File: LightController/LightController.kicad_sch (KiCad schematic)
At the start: 0 parts

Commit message: Add the funky stuff to start.  This will be hell btw.
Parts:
- added J1: RJ45, symbol Connector:RJ45
- added Q1: BSS138, Package_TO_SOT_SMD:SOT-23, symbol Transistor_FET:BSS138
- added Q2, Q3, Q4, Q5, Q6, Q7: Q_NMOS_GDS, Package_TO_SOT_THT:TO-220-3_Vertical, symbol Device:Q_NMOS_GDS
- added R1, R2: 10k, symbol Device:R_US
- added R3, R4, R5, R6, R7, R8: 330ohm, symbol Device:R_US
- added U1: ESP32-WROOM-32D, RF_Module:ESP32-WROOM-32, symbol RF_Module:ESP32-WROOM-32D
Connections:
- new net: Q5.1 (G), R6.2
- new net: Q6.1 (G), R7.2
- new net: Q3.1 (G), R4.2
- new net: Q7.1 (G), R8.2
- new net: Q2.1 (G), R3.2
- new net: Q4.1 (G), R5.2
- new net GND: Q1.2 (S), Q1.3 (D), R1.2, R2.2, U1.1 (GND), U1.15 (GND), U1.38 (GND), U1.39 (GND)
- new net STATUS_LED: Q1.1 (G), R1.1, U1.12 (IO27)
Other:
- note added: "12V to 3.3V for ESP32"
- note added: "Main Brain"
- note added: "Output Channels"
- note added: "RS485 Comms"
- note added: "Sig/Pwr Input"
- note added: "Status LED Output (there is no 5v source on this board hahaha fuck!)"
- note added: "https://forum.arduino.cc/t/logic-level-converter-schematic/523295"
- company: (none) -> Garden State Combat Robotics League
- title: (none) -> LED Channel Controller

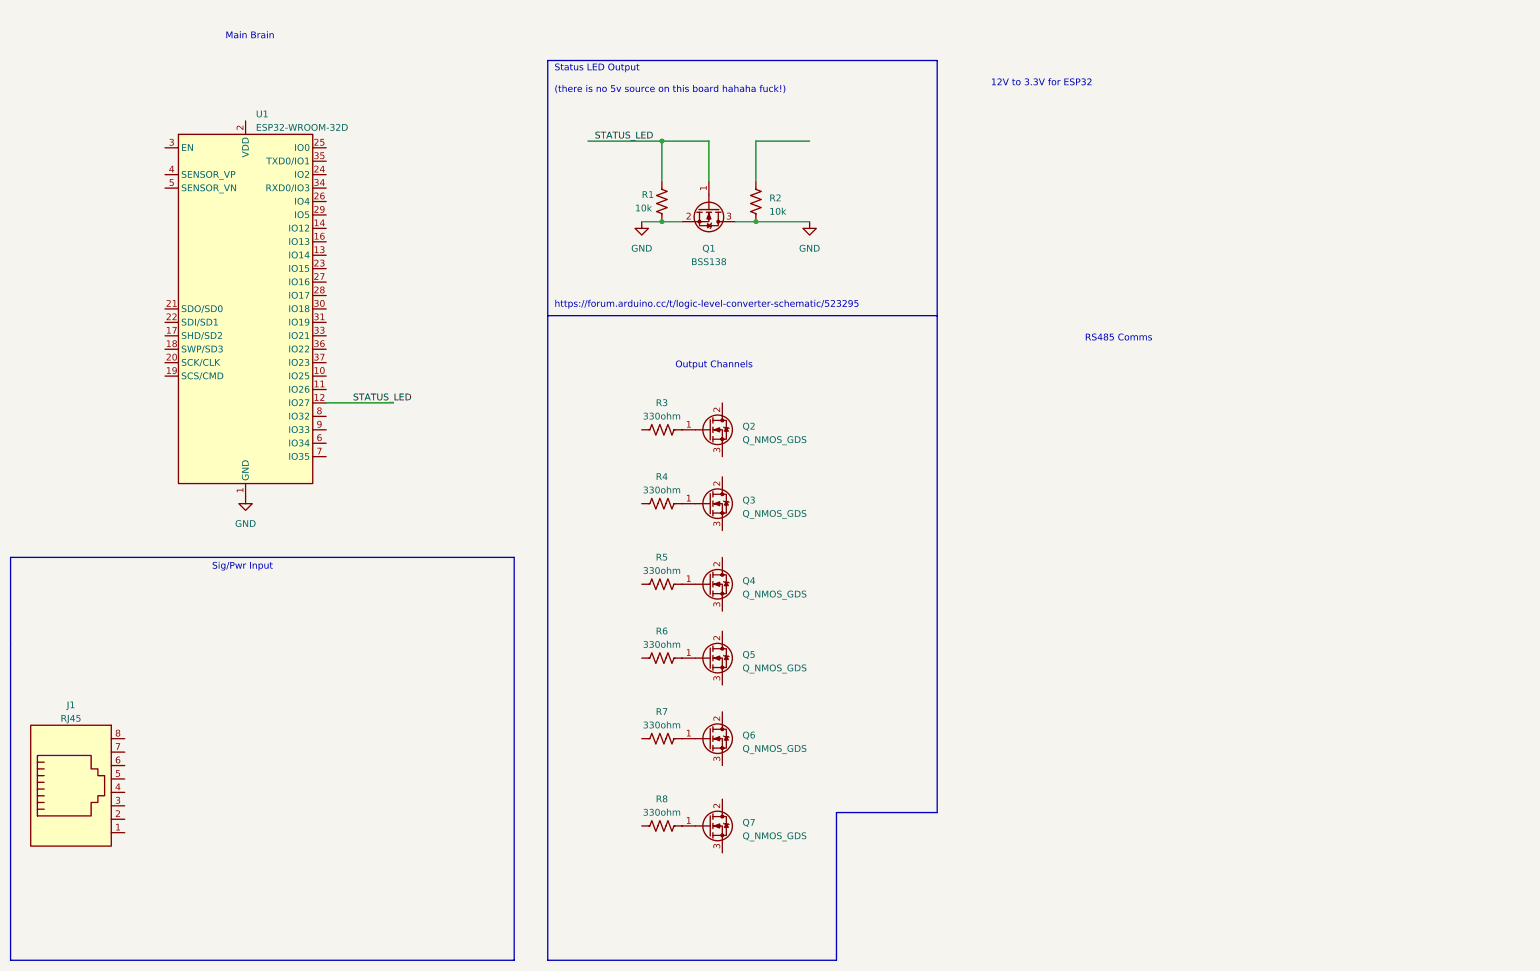
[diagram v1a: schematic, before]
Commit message: Updated first half of schematic, mostlyish.  Lots to go for lighting.
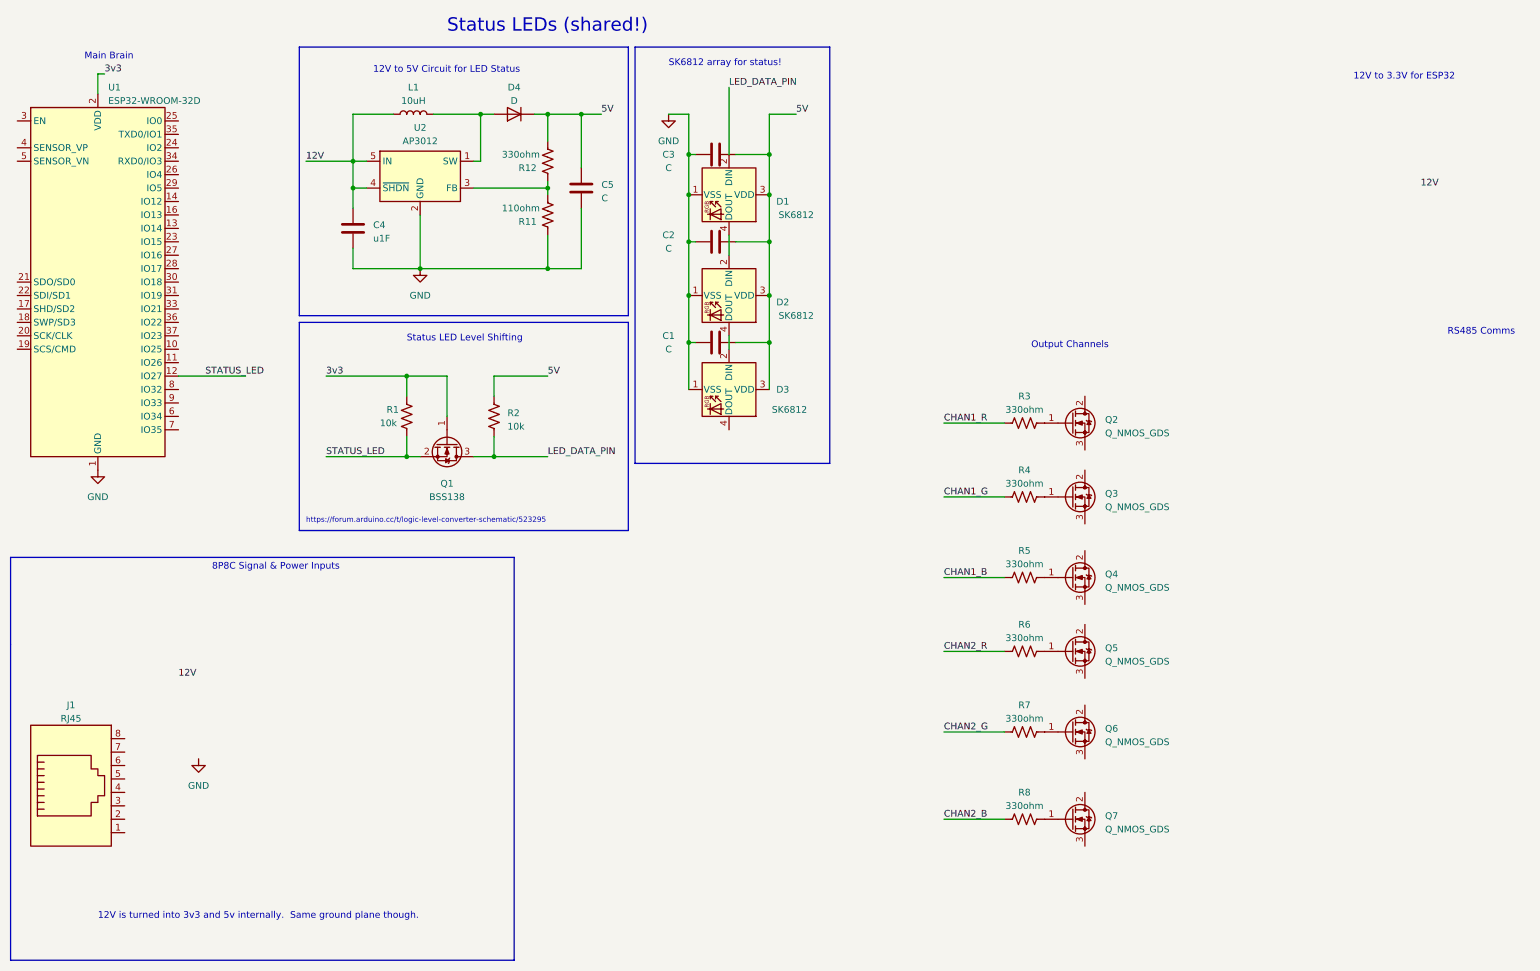
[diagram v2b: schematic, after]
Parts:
- added C1, C2, C3, C5: C, symbol Device:C
- added C4: u1F, symbol Device:C
- added D1, D2, D3: SK6812, LED_SMD:LED_SK6812_PLCC4_5.0x5.0mm_P3.2mm, symbol LED:SK6812
- added D4: D, symbol Device:D
- added L1: 10uH, symbol Device:L
- added R11: 110ohm, symbol Device:R_US
- added R12: 330ohm, symbol Device:R_US
- added U2: AP3012, Package_TO_SOT_SMD:SOT-23-5, symbol Regulator_Switching:AP3012
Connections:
- net GND: now also C1.1, C2.1, C3.1, C4.2, C5.1, D1.1 (VSS), D2.1 (VSS), D3.1 (VSS), R11.1, U2.2 (GND); no longer Q1.2 (S), Q1.3 (D), R1.2, R2.2
- net STATUS_LED: now also Q1.2 (S), R1.2; no longer Q1.1 (G), R1.1
- net CHAN2_G: now reaches R7.1
- net CHAN1_G: now reaches R4.1
- net 3v3: now reaches U1.2 (VDD)
- net 3v3: now also Q1.1 (G), R1.1
- net 5V: now reaches R2.1
- net 5V: now also C1.2, C2.2, C3.2, C5.2, D1.3 (VDD), D2.3 (VDD), D3.3 (VDD), D4.1 (K), R12.2
- net CHAN1_R: now reaches R3.1
- net CHAN2_B: now reaches R8.1
- net CHAN1_B: now reaches R5.1
- net CHAN2_R: now reaches R6.1
- new net: D4.2 (A), L1.2, U2.1 (SW)
- new net: D1.4 (DOUT), D2.2 (DIN)
- new net: D2.4 (DOUT), D3.2 (DIN)
- new net: R11.2, R12.1, U2.3 (FB)
- new net 12V: C4.1, L1.1, U2.4 (~{SHDN}), U2.5 (IN)
- new net LED_DATA_PIN: D1.2 (DIN), Q1.3 (D), R2.2
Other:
- note added: "12V is turned into 3v3 and 5v internally. Same ground plane though."
- note added: "12V to 5V Circuit for LED Status"
- note added: "8P8C Signal & Power Inputs"
- note added: "SK6812 array for status!"
- note added: "Status LED Level Shifting"
- note added: "Status LEDs (shared!)"
- note removed: "Sig/Pwr Input"
- note removed: "Status LED Output (there is no 5v source on this board hahaha fuck!)"
- moved on the sheet: Q1, Q2, Q3, Q4, Q5, Q6, Q7, R1, R2, R3, R4, R5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

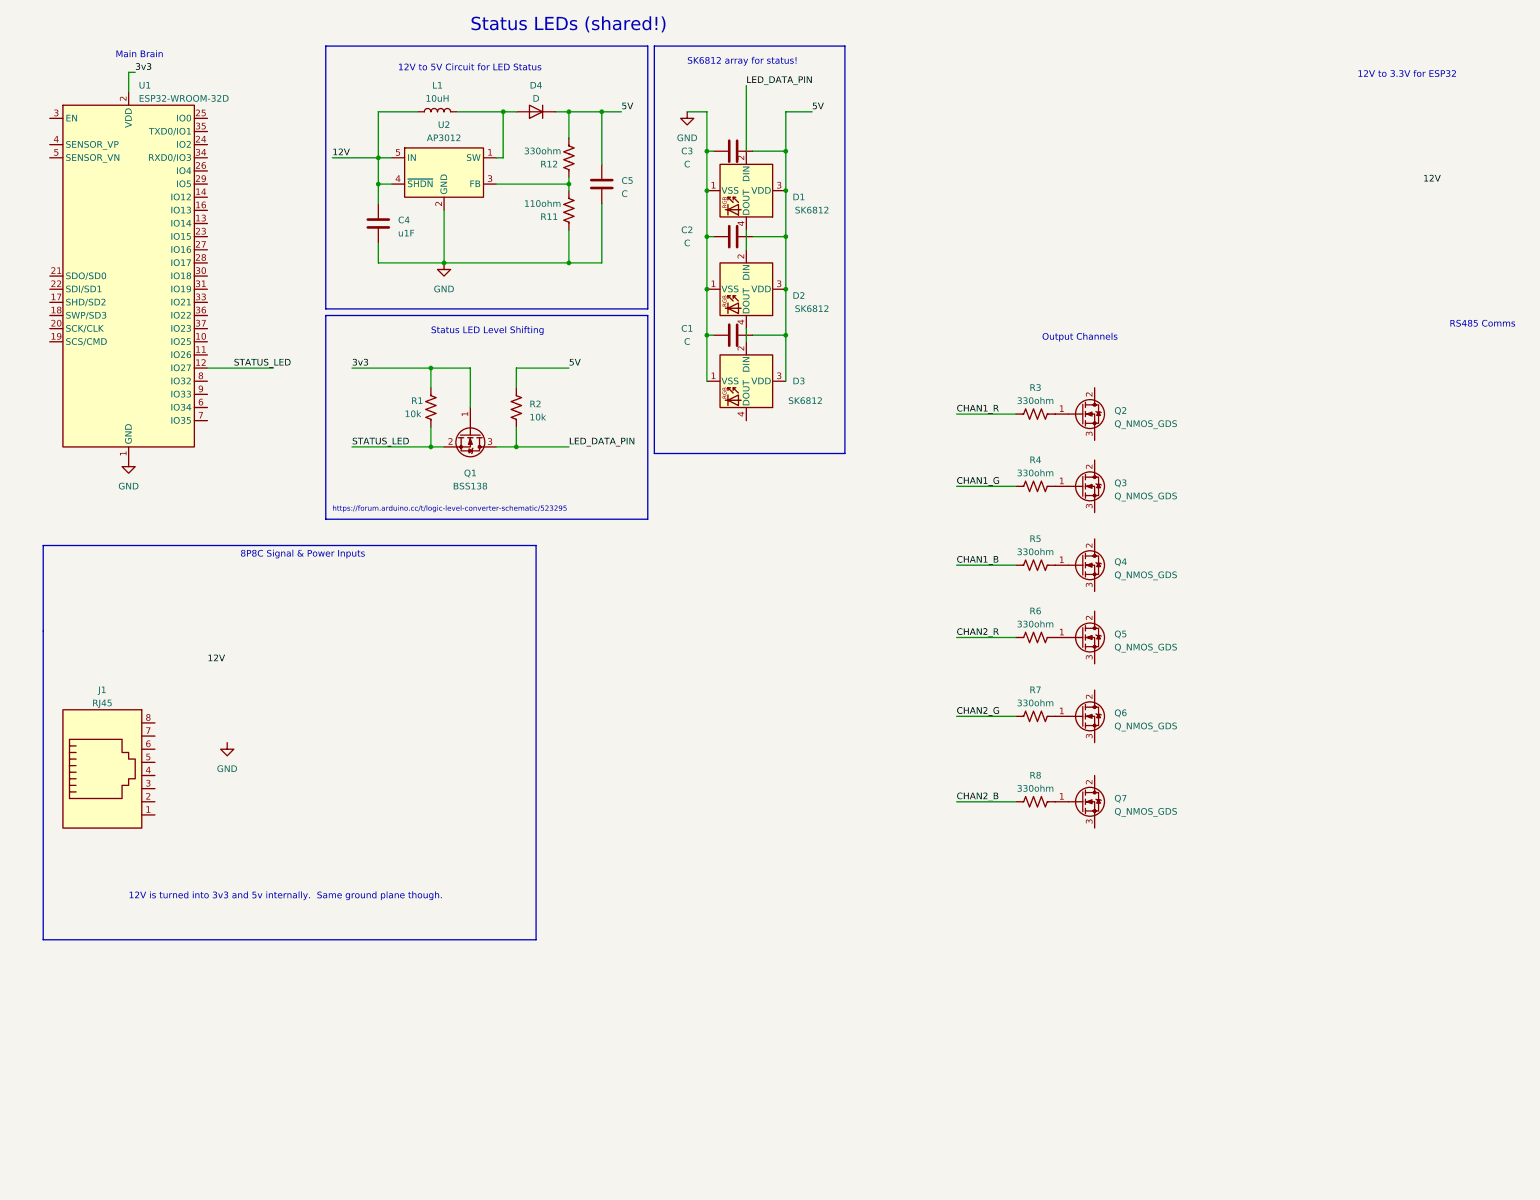
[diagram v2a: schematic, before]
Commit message: Update roughly, using the same schematic for the 3v3 and 5v stuff, still need to figure out values, etc.
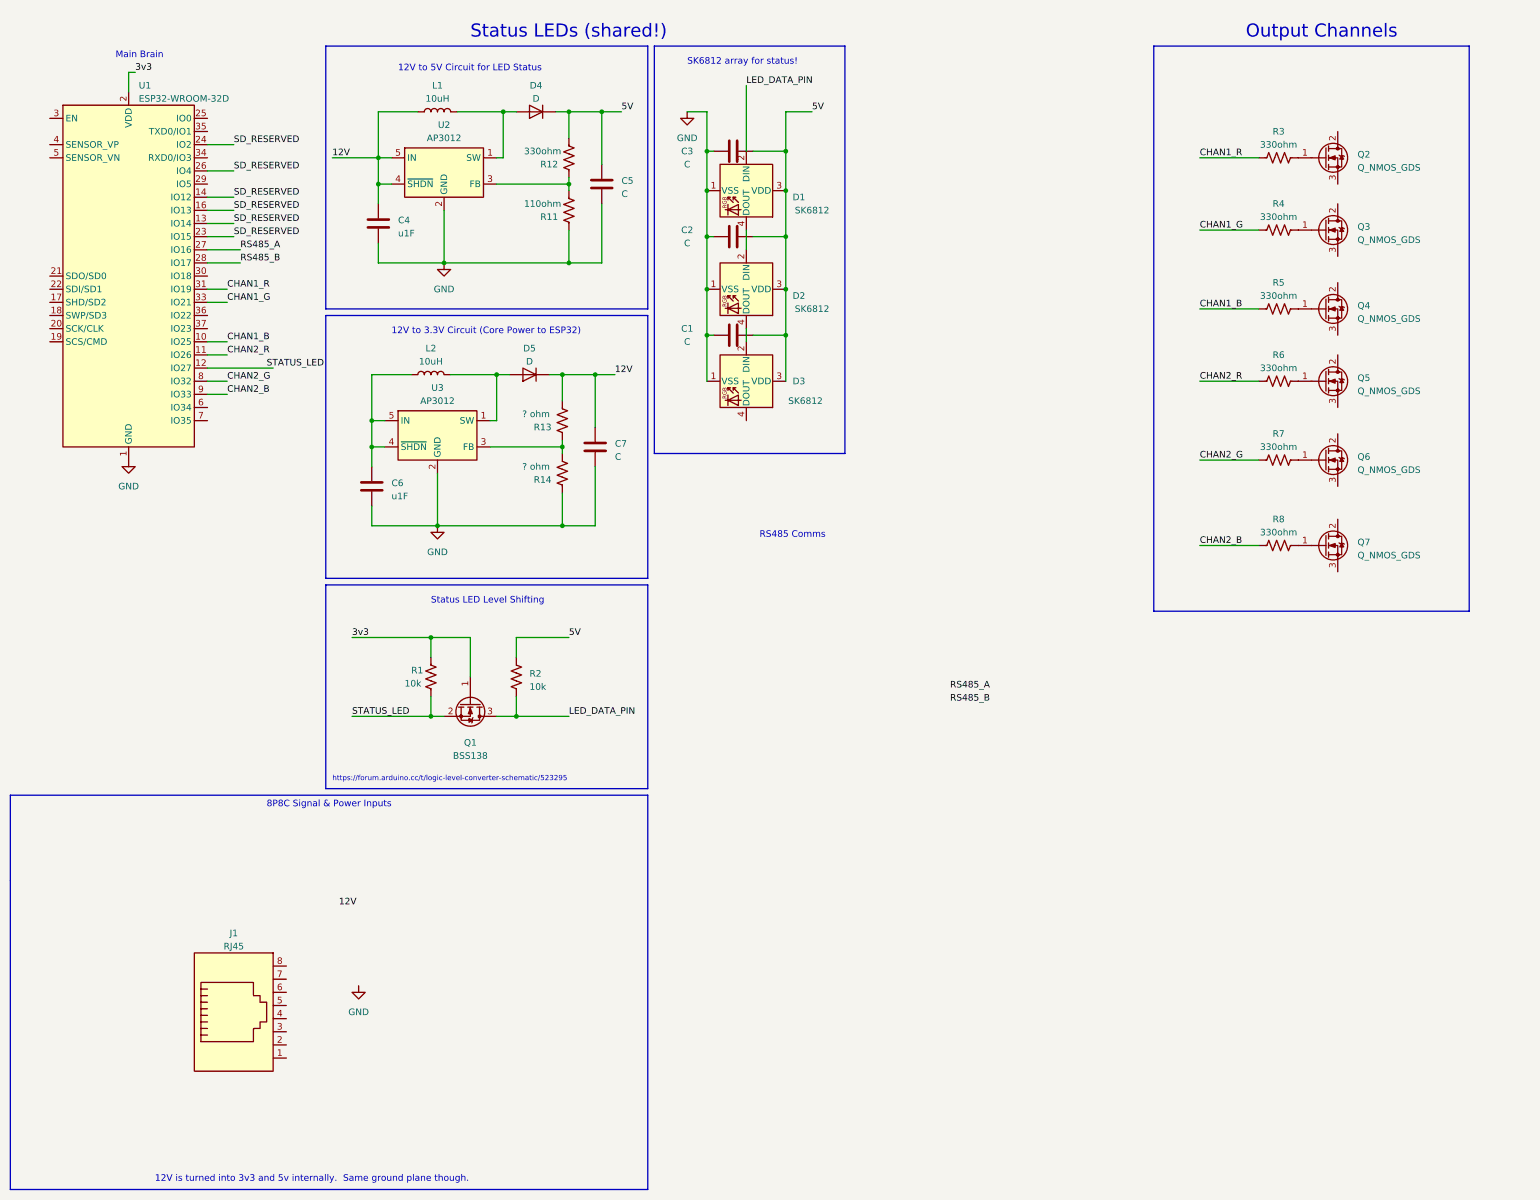
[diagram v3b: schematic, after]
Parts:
- added C6: u1F, symbol Device:C
- added C7: C, symbol Device:C
- added D5: D, symbol Device:D
- added L2: 10uH, symbol Device:L
- added R13, R14: ? ohm, symbol Device:R_US
- added U3: AP3012, Package_TO_SOT_SMD:SOT-23-5, symbol Regulator_Switching:AP3012
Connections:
- net 12V: now also C7.2, D5.1 (K), R13.2
- net CHAN1_B: now also U1.10 (IO25)
- net CHAN1_G: now also U1.33 (IO21)
- net CHAN1_R: now also U1.31 (IO19)
- net CHAN2_B: now also U1.9 (IO33)
- net CHAN2_G: now also U1.8 (IO32)
- net CHAN2_R: now also U1.11 (IO26)
- net GND: now also C6.2, C7.1, R14.1, U3.2 (GND)
- net SD_RESERVED: now reaches U1.13 (IO14)
- net SD_RESERVED: now also U1.14 (IO12), U1.16 (IO13), U1.23 (IO15), U1.24 (IO2), U1.26 (IO4)
- net RS485_A: now reaches U1.27 (IO16)
- net RS485_B: now reaches U1.28 (IO17)
- new net: R13.1, R14.2, U3.3 (FB)
- new net: D5.2 (A), L2.2, U3.1 (SW)
- new net: C6.1, L2.1, U3.4 (~{SHDN}), U3.5 (IN)
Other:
- note added: "12V to 3.3V Circuit (Core Power to ESP32)"
- note removed: "12V to 3.3V for ESP32"
- moved on the sheet: J1, Q1, Q2, Q3, Q4, Q5, Q6, Q7, R1, R2, R3, R4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

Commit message: Add footprints and shit.
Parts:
- added C8: 10uF, Capacitor_SMD:C_1206_3216Metric, symbol Device:C
- added C9: .1uF, Capacitor_SMD:C_1206_3216Metric, symbol Device:C
- added J2, J3: Conn_01x04, Connector_PinSocket_2.54mm:PinSocket_1x04_P2.54mm_Vertical, symbol Connector_Generic:Conn_01x04
- added R10, R9: 20k ohm, symbol Device:R_US
- added R15: 120 ohm, symbol Device:R_US
- added R16, R17, R18, R19: 10k ohm, symbol Device:R_US
- added U4: MAX485E, Package_SO:SOP-8_3.9x4.9mm_P1.27mm, symbol Interface_UART:MAX485E
- C1, C2, C3, C4, C6: footprint (none) -> Capacitor_SMD:C_1206_3216Metric
- C5, C7: value C -> 1uF; footprint (none) -> Capacitor_SMD:C_1206_3216Metric
- D4, D5: footprint (none) -> Diode_SMD:D_1206_3216Metric_Pad1.42x1.75mm_HandSolder
- L1, L2: footprint (none) -> Inductor_SMD:L_1210_3225Metric_Pad1.42x2.65mm_HandSolder
- R11, R12: footprint (none) -> Resistor_SMD:R_1206_3216Metric
- R13: value ? ohm -> 330 ohm; footprint (none) -> Resistor_SMD:R_1206_3216Metric
- R14: value ? ohm -> 200 ohm; footprint (none) -> Resistor_SMD:R_1206_3216Metric
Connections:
- net 12V: now also J1.7, J1.8, J2.1 (Pin_1), J3.1 (Pin_1)
- net 3v3: now also C8.1, C9.1, R10.2, R16.1, R17.1, R17.2, R18.1, R18.2, R19.1, U4.2 (~{RE}), U4.3 (DE), U4.8 (VCC)
- net GND: now also J1.1, J1.2, Q2.3 (S), Q3.3 (S), Q4.3 (S), Q5.3 (S), Q6.3 (S), Q7.3 (S), C8.2, C9.2, R9.1, U4.5 (GND)
- net RS485_A: now also R16.2, U4.1 (RO)
- net RS485_B: now also R19.2, U4.4 (DI)
- net at Q5.2 (D): now also J3.2 (Pin_2)
- net MAX485_B: now reaches J1.3
- net MAX485_B: now also R10.1, R15.2, U4.6 (A)
- net MAX485_A: now reaches J1.6
- net MAX485_A: now also R15.1, R9.2, U4.7 (B)
- net at Q7.2 (D): now also J3.4 (Pin_4)
- net at Q6.2 (D): now also J3.3 (Pin_3)
- net at Q2.2 (D): now also J2.2 (Pin_2)
- net at Q4.2 (D): now also J2.4 (Pin_4)
- net at Q3.2 (D): now also J2.3 (Pin_3)
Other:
- moved on the sheet: Q2, Q3, Q4, Q5, Q6, Q7, R3, R4, R5, R6, R7, R8
